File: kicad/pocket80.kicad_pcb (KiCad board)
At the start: 4 copper layers, 68.6 x 107.3 mm, 140 parts, among them J1 USB_C_Receptacle_USB2.0_14P, J2 Conn_02x10_Odd_Even, J3 Conn_01x02, Q1 IRLML6402, Q2 BC847, SW1 F1, SW10 4, SW11 9, SW12 5, SW13 A, SW14 6, SW15 B, SW16 7, SW17 0, SW18 INC, SW19 1, SW2 F2, SW20 DEC, SW21 2, SW22 SEL, SW23 3, SW24 GO!, SW25 SW_Push_DPDT, SW26 RESET, SW3 F3, SW4 F4, SW5 C, SW6 D, SW7 E, SW8 F, SW9 8, U1 Z80CPU, U10 74HC00, U11 74HC138, U12 CH340N, U13 TP4056-42-ESOP8, U14 SX1308, U15 LM393, U16 74HC74, U17 28C256, U2 74HC244, U3 Z80 PIO, U4 Z80 SIO3, U5 Z80 CTC, U6 NE555D, U7 74HC04, U8 62256, U9 24C512, Y1 3.6864M

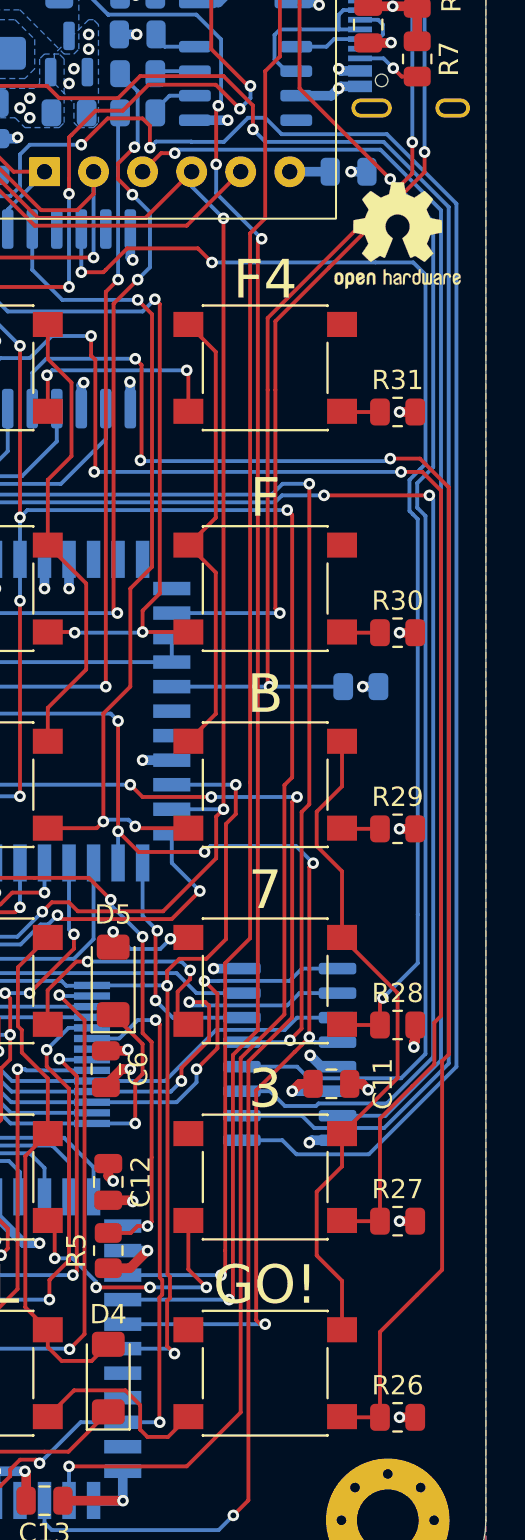
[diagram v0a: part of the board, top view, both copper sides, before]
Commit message: HW: Fix lack of /WR gating for DL1414
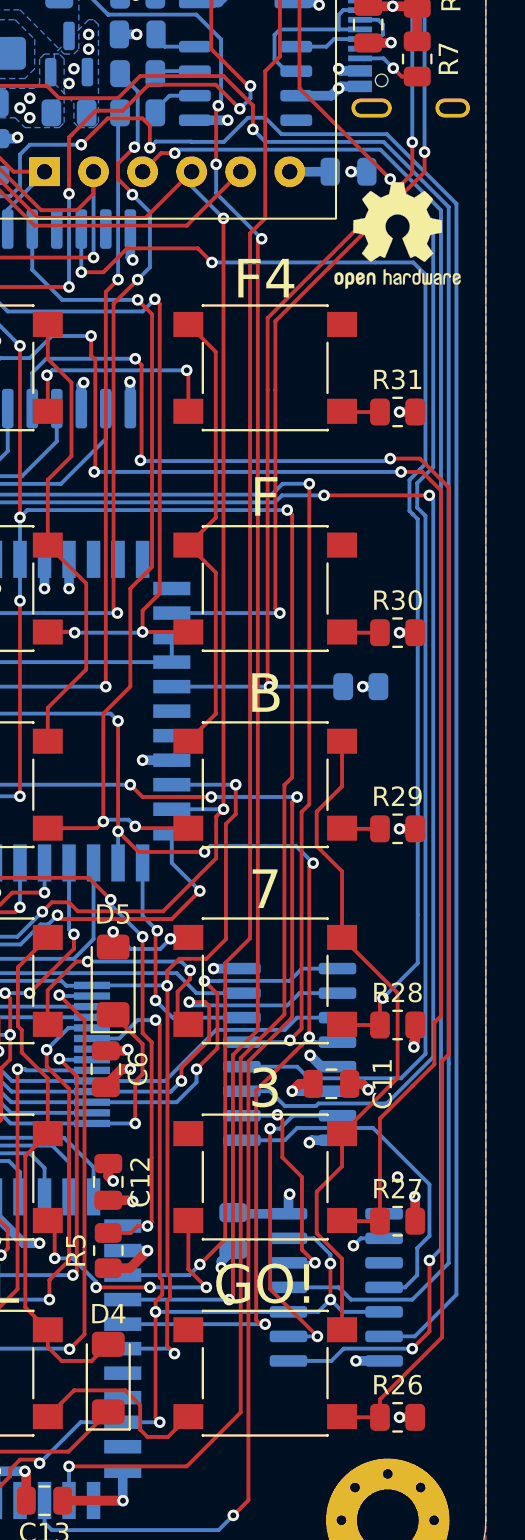
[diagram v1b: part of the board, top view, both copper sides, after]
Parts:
- added C32: 100n, Capacitor_SMD:C_0805_2012Metric, B.Cu at (152.0, 122.4)
- added U18: 74HC32, Package_SO:SO-14_3.9x8.65mm_P1.27mm, B.Cu at (157.4, 125.3)
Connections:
- DL1 pad 3: /CPU/~{DISP1} -> Net-(DL1-~{WR})
- DL2 pad 3: /CPU/~{DISP2} -> Net-(DL2-~{WR})
- DL3 pad 3: /CPU/~{DISP3} -> Net-(DL3-~{WR})
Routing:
- net Net-(DL1-~{WR}): track 0.00 -> 124.7 mm, vias 0 -> 2
- net /CPU/~{DISP1}: track 117.3 -> 11.7 mm
- net Net-(DL2-~{WR}): track 0.00 -> 102.1 mm, vias 0 -> 2
- net Net-(DL3-~{WR}): track 0.00 -> 83.5 mm, vias 0 -> 3
- net /CPU/~{DISP2}: track 99.0 -> 18.1 mm, vias 2 -> 0
- net /CPU/~{DISP3}: track 67.8 -> 17.0 mm, vias 1 -> 2
- net /CPU/~{WR}: track 58.3 -> 75.7 mm, vias 4 -> 7
- net GND: track 114.9 -> 120.6 mm, vias 69 -> 73
- net VCC: track 121.6 -> 126.0 mm, vias 46 -> 47
- net Net-(U1-~{HALT}): track 102.0 -> 101.0 mm

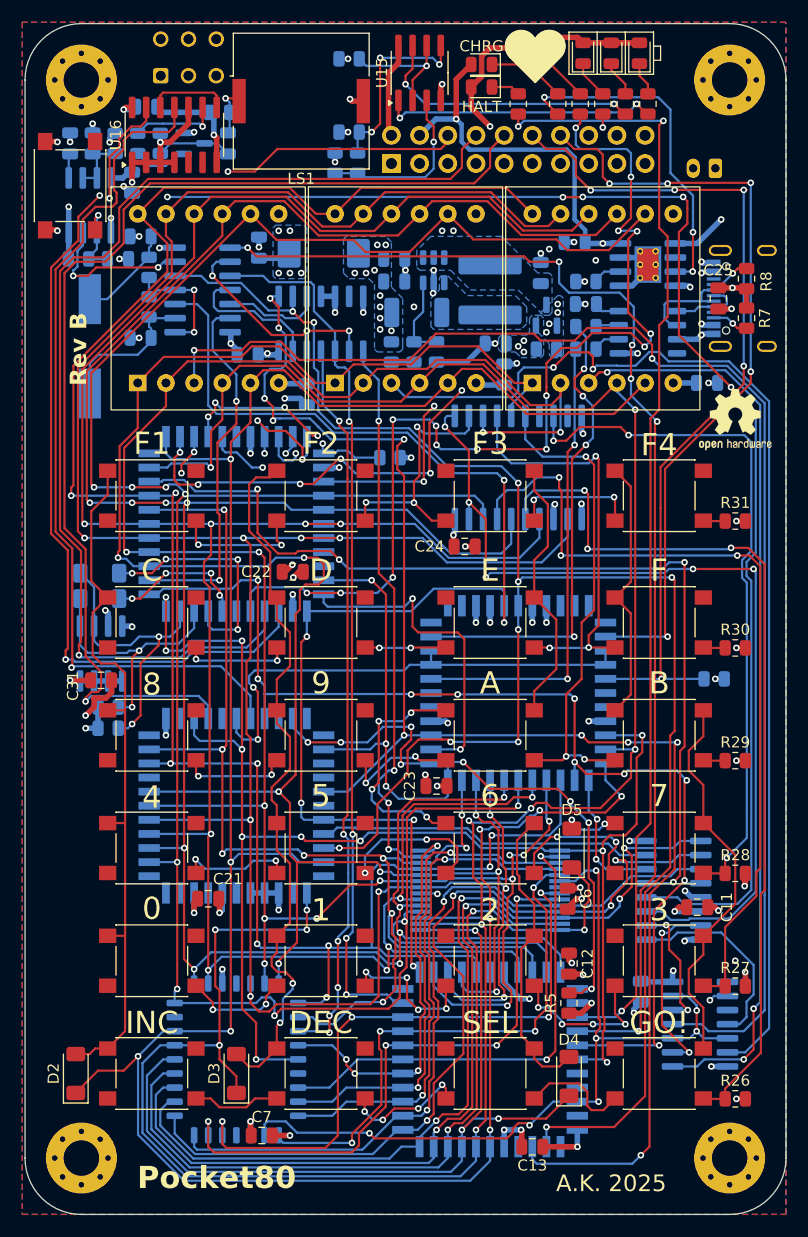
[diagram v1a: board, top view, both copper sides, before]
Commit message: HW: Mechanical improvement
- move USB invards to clear the case,
- extend expansion connector to be flush with the case.
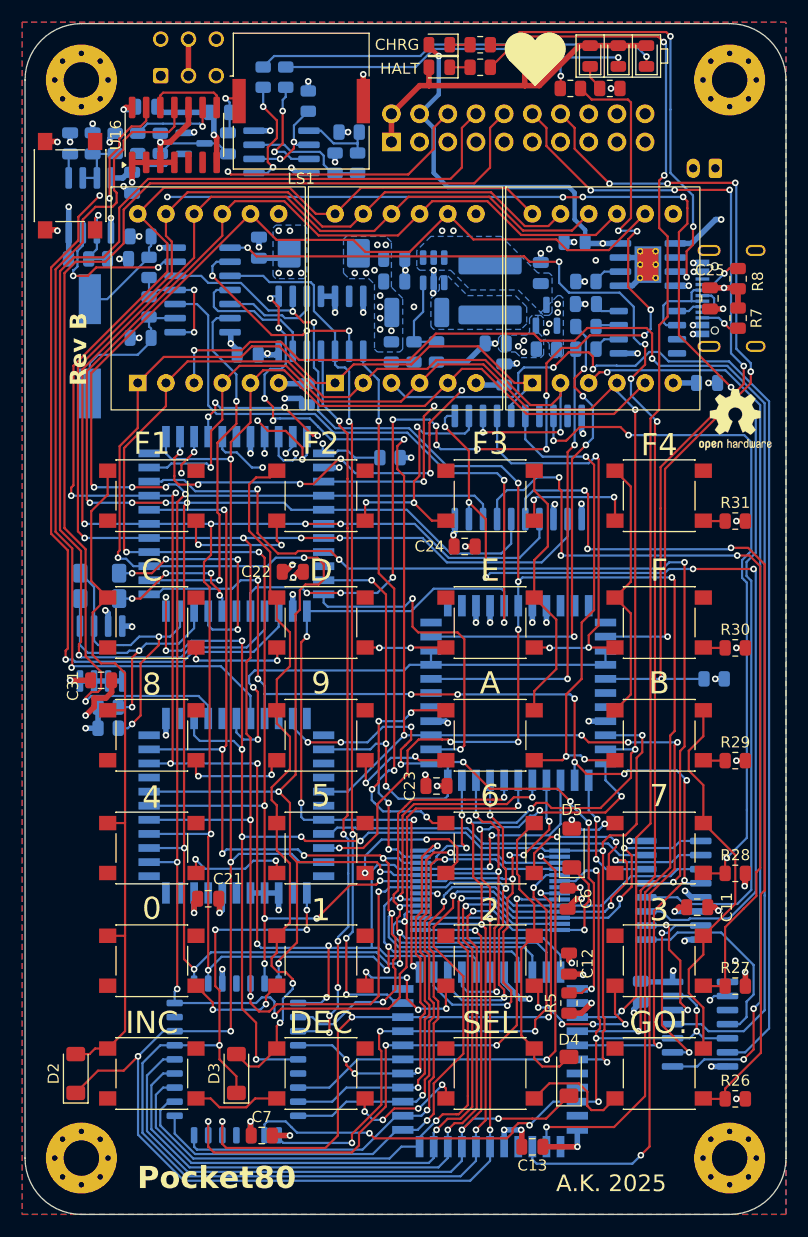
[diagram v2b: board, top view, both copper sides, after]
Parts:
- R22, R23, U15: moved to B.Cu
- moved R22 34.8 mm to (118.0, 40.0)
- moved R23 30.7 mm to (120.0, 40.0)
- moved U15 14.3 mm to (119.6, 46.7), turned to 0 degrees
- moved R11 8.79 mm to (137.5, 37.1), turned to 0 degrees
- moved R21 5.30 mm to (122.0, 42.2), turned to -90 degrees
- moved R6 4.76 mm to (137.5, 39.1), turned to 0 degrees
- moved D1 4.20 mm to (133.9, 39.1)
- moved D6 4.20 mm to (133.9, 37.1)
- moved J2 1.94 mm to (129.5, 45.8)
- moved R35 1.66 mm to (145.7, 41.0), turned to 0 degrees
- moved R17 1.53 mm to (149.2, 41.0), turned to 0 degrees
- moved J1 1.02 mm to (161.3, 59.9)
- moved C25 0.76 mm to (158.2, 59.9)
- moved R7 0.76 mm to (160.8, 61.7)
- moved R8 0.76 mm to (160.8, 58.2)
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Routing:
- net Net-(D9-K): track 3.04 -> 36.7 mm, vias 0 -> 1
- net Net-(D10-K): track 3.25 -> 31.8 mm, vias 0 -> 1
- net Net-(R23-Pad2): track 24.7 -> 9.61 mm
- net Net-(R22-Pad2): track 24.9 -> 10.2 mm
- net Net-(U15B-+): track 17.4 -> 6.80 mm, vias 3 -> 0
- net Net-(U13-~{CHRG}): track 30.8 -> 41.0 mm
- net Net-(U1-~{HALT}): track 101.0 -> 110.9 mm
- net Net-(D6-K): track 7.02 -> 1.83 mm
- net Net-(U15A-+): track 15.8 -> 10.9 mm, vias 1 -> 0
- net Net-(Q1-G): track 0.00 -> 3.30 mm
- net Net-(U15A--): track 12.0 -> 9.34 mm, vias 1 -> 2
- net VCC: track 126.0 -> 128.6 mm
- net GND: track 120.6 -> 118.3 mm
- net /Expansion/ARDY: track 49.2 -> 51.4 mm
- net /Expansion/~{ASTB}: track 52.1 -> 54.2 mm
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
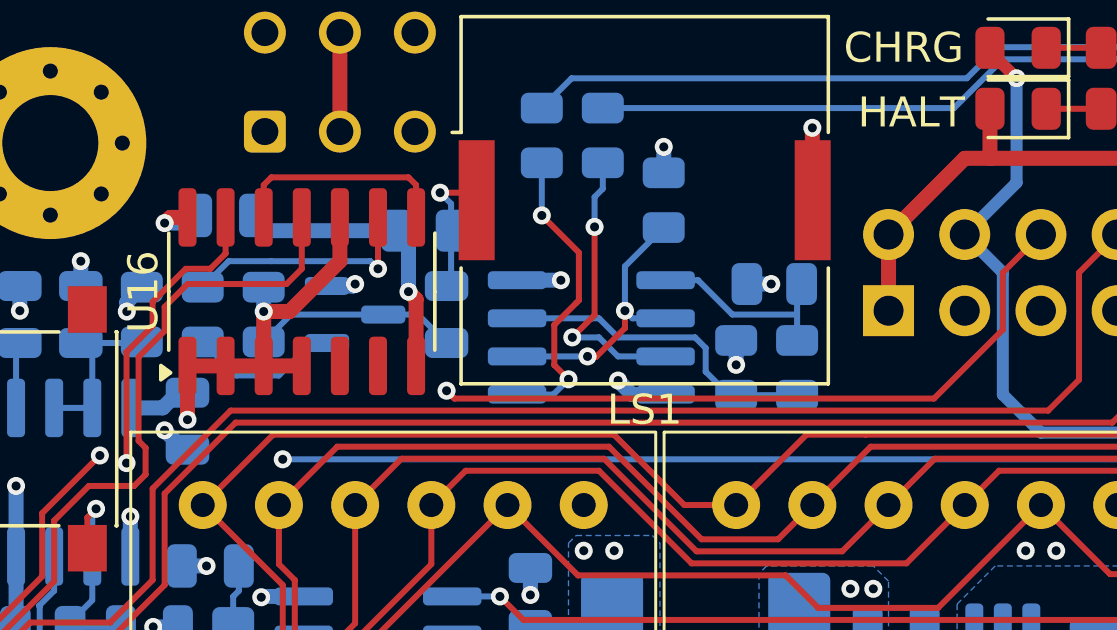
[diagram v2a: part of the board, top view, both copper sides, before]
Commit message: HW: add piezo power filter
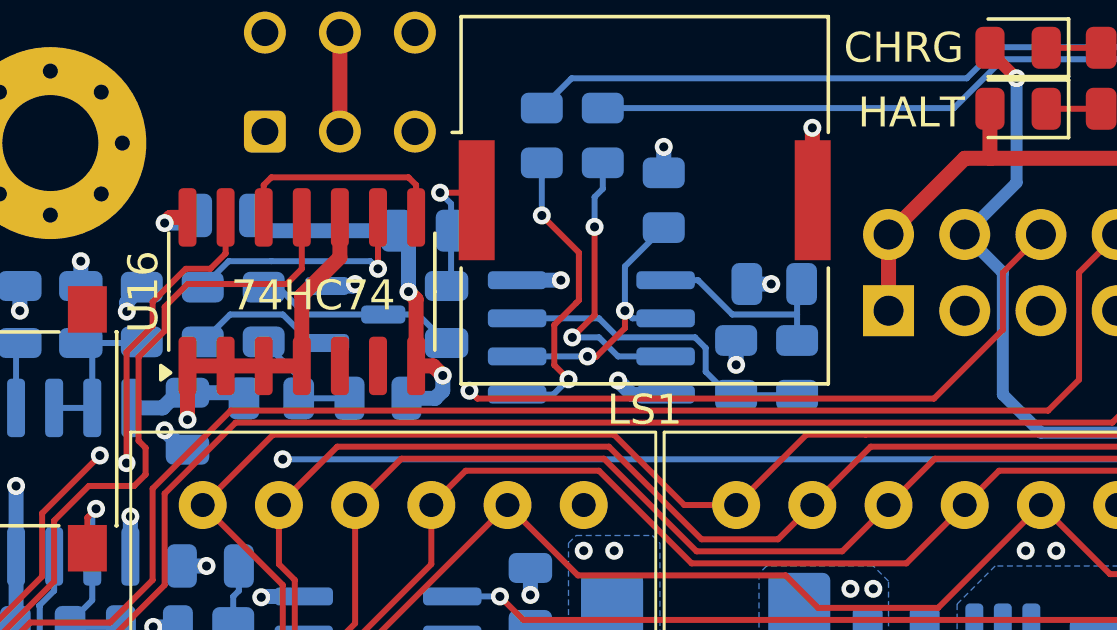
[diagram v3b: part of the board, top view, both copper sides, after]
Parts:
- added C33: 2u2, Capacitor_SMD:C_0805_2012Metric, B.Cu at (112.5, 48.8)
- added R38: 510R, Resistor_SMD:R_0805_2012Metric, B.Cu at (109.0, 48.8)
- R32: value 100k -> 10K
- turned R24 to 90 degrees
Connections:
- R24 pad 1: VCC -> Net-(C33-Pad1)
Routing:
- net Net-(C33-Pad1): track 0.00 -> 4.06 mm
- net GND: track 118.3 -> 121.2 mm, vias 73 -> 74
- net VCC: track 128.6 -> 128.7 mm, vias 47 -> 46
